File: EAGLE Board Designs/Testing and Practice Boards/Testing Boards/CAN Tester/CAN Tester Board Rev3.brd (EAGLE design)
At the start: 44.1 x 43.2 mm, 10 parts, among them J1 CONNECTOR-CAN_μF_S_RA_, J2 CONNECTOR-2_MICROFIT_SMD_RIGH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, U1 MCP2562FD

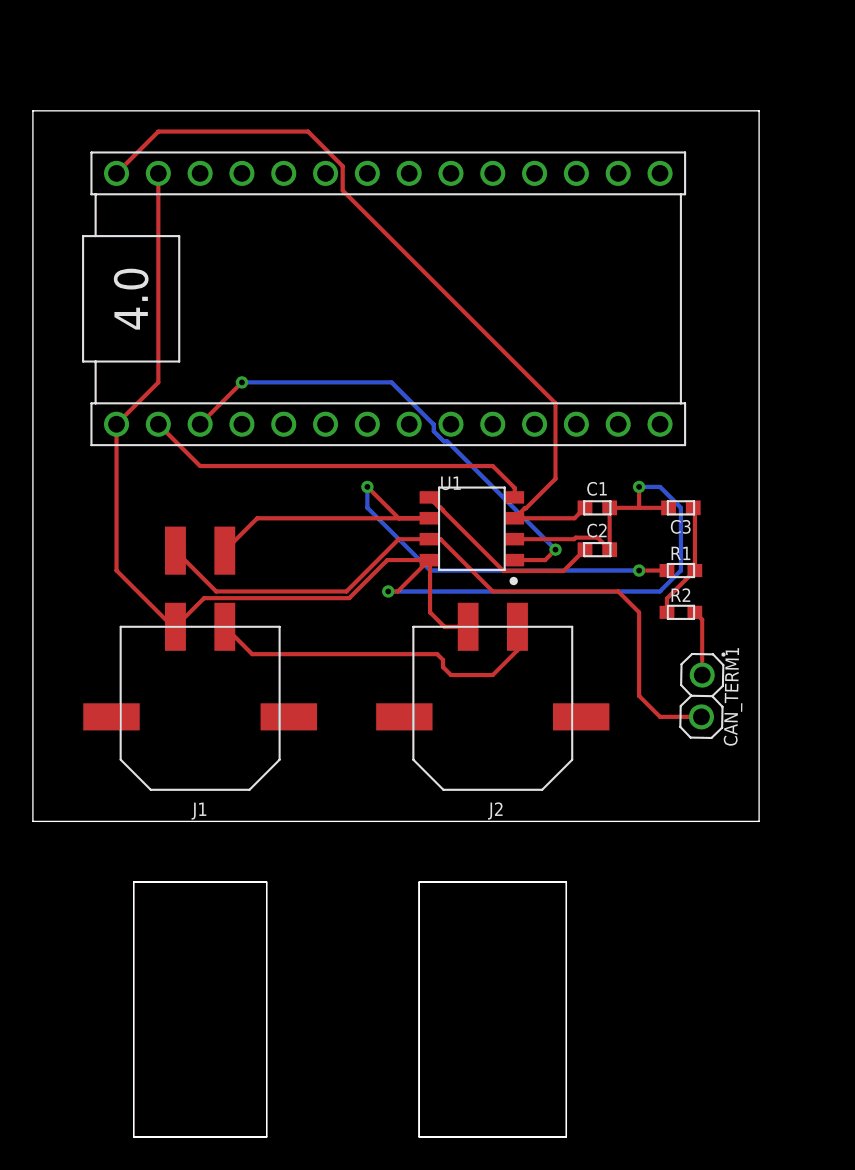
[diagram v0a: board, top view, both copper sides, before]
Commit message: added lin reg
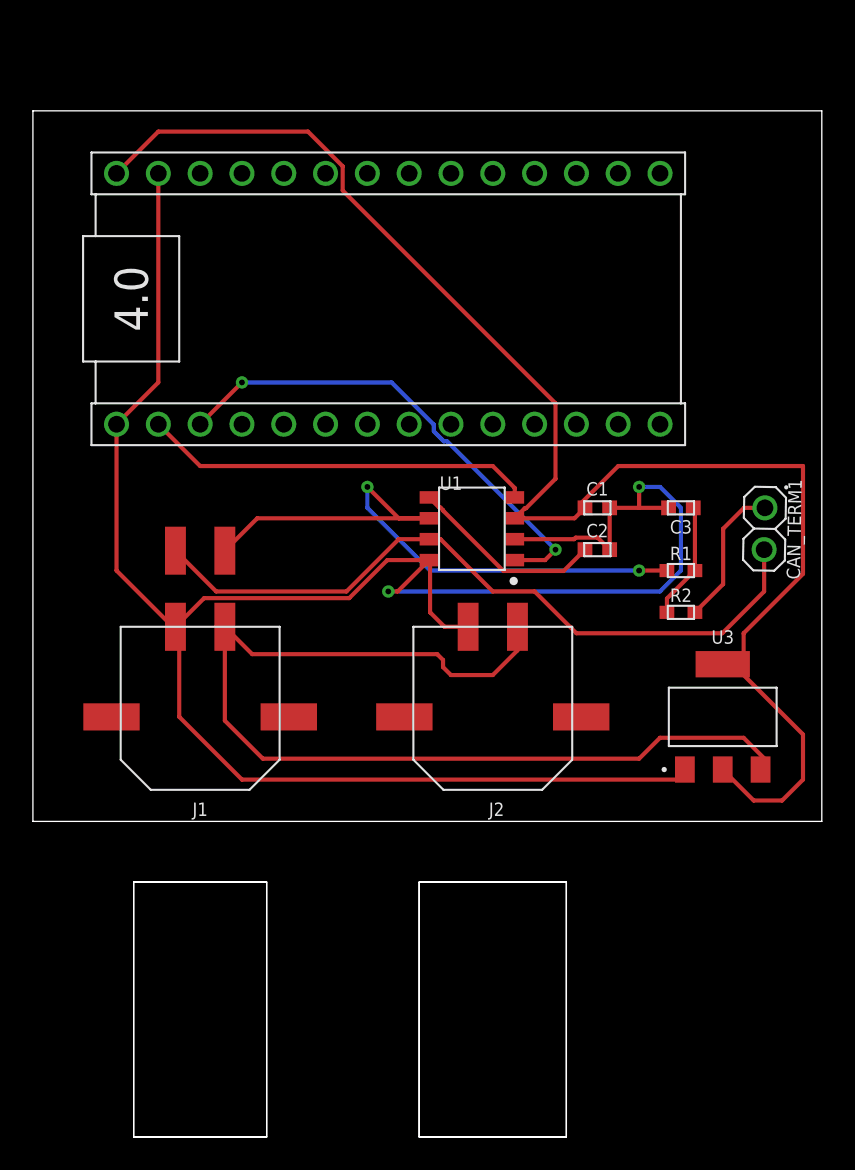
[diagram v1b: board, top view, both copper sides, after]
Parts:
- added U3: VOLTAGE_REGULATOR_SOT-223_3.3V, HyTechDevices:SOT-223
- moved CAN_TERM1 10.9 mm to (44.5, 54.6)
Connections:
- net +12V: now also U3.3
- net +5V: now also U3.2, U3.4
- net GND: now also U3.1
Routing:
- net +5V: track 48.0 -> 91.2 mm
- net +12V: track 21.3 -> 61.8 mm
- net GND: track 95.1 -> 133.4 mm
- net N$5: track 3.99 -> 8.86 mm
- net CANH: track 41.7 -> 44.1 mm
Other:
- board size 44.1 x 43.2 mm -> 47.9 x 43.2 mm
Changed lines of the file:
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@@
 <board>
 <plain>
-<wire x1="0" y1="36.83" x2="44.12" y2="36.83" width="0" layer="20"/>
-<wire x1="44.12" y1="36.83" x2="44.12" y2="80" width="0" layer="20"/>
-<wire x1="44.12" y1="80" x2="0" y2="80" width="0" layer="20"/>
+<wire x1="0" y1="36.83" x2="47.93" y2="36.83" width="0" layer="20"/>
+<wire x1="47.93" y1="36.83" x2="47.93" y2="80" width="0" layer="20"/>
+<wire x1="47.93" y1="80" x2="0" y2="80" width="0" layer="20"/>
 <wire x1="0" y1="80" x2="0" y2="36.83" width="0" layer="20"/>
 </plain>
@@
 <attribute name="VOLTAGE" value="10V" x="10.16" y="95.25" size="1.778" layer="27" rot="R180" display="off"/>
 </element>
-<element name="CAN_TERM1" library="HyTechDevices_Jumper" package="1X02" value="JUMPER__1X02" x="40.64" y="44.45" smashed="yes" rot="R268.9">
-<attribute name="DKPN" value="WM23656-ND" x="0.96030625" y="28.69884375" size="1.778" layer="27" rot="R268.9" display="off"/>
-<attribute name="MANUFACTURER" value="Molex" x="0.96030625" y="28.69884375" size="1.778" layer="27" rot="R268.9" display="off"/>
-<attribute name="MOPN" value="538-90120-1082" x="0.96030625" y="28.69884375" size="1.778" layer="27" rot="R268.9" display="off"/>
-<attribute name="MPN" value="90120-1082 " x="0.96030625" y="28.69884375" size="1.778" layer="27" rot="R268.9" display="off"/>
-<attribute name="NAME" x="42.03674375" y="44.423178125" size="0.8128" layer="25" font="vector" rot="R268.9" align="bottom-center"/>
+<element name="CAN_TERM1" library="HyTechDevices_Jumper" package="1X02" value="JUMPER__1X02" x="44.45" y="54.61" smashed="yes" rot="R268.9">
+<attribute name="DKPN" value="WM23656-ND" x="4.77030625" y="38.85884375" size="1.778" layer="27" rot="R268.9" display="off"/>
+<attribute name="MANUFACTURER" value="Molex" x="4.77030625" y="38.85884375" size="1.778" layer="27" rot="R268.9" display="off"/>
+<attribute name="MOPN" value="538-90120-1082" x="4.77030625" y="38.85884375" size="1.778" layer="27" rot="R268.9" display="off"/>
+<attribute name="MPN" value="90120-1082 " x="4.77030625" y="38.85884375" size="1.778" layer="27" rot="R268.9" display="off"/>
+<attribute name="NAME" x="45.84674375" y="54.583178125" size="0.8128" layer="25" font="vector" rot="R268.9" align="bottom-center"/>
 </element>
 <element name="R1" library="HyTechDevices" package="0603-RES" value="RESISTOR_0603_60.4" x="39.37" y="52.07" smashed="yes">
@@
 <attribute name="MPN" value="0436500214" x="27.94" y="43.18" size="1.778" layer="27" display="off"/>
 <attribute name="NAME" x="28.1686" y="37.973" size="0.8128" layer="25" rot="R180" align="bottom-center"/>
+</element>
+<element name="U3" library="HyTechDevices" package="SOT-223" value="VOLTAGE_REGULATOR_SOT-223_3.3V" x="41.91" y="43.18" smashed="yes">
+<attribute name="DKPN" value="LMS8117AMP-3.3/NOPBCT-ND" x="41.91" y="43.18" size="1.778" layer="27" display="off"/>
+<attribute name="MANUFACTURER" value="Texas Instruments" x="41.91" y="43.18" size="1.778" layer="27" display="off"/>
+<attribute name="MOPN" value="926-LMS8117AMP33NOPB" x="41.91" y="43.18" size="1.778" layer="27" display="off"/>
+<attribute name="MPN" value="LMS8117AMP-3.3/NOPB" x="41.91" y="43.18" size="1.778" layer="27" display="off"/>
+<attribute name="NAME" x="41.91" y="47.625" size="0.8128" layer="25" font="vector" align="bottom-center"/>
 </element>
 </elements>
@@
 <wire x1="39.37" y1="55.88" x2="38.1" y2="57.15" width="0.254" layer="16"/>
 <wire x1="38.1" y1="57.15" x2="36.83" y2="57.15" width="0.254" layer="16"/>
+<contactref element="U3" pad="1"/>
+<wire x1="8.66" y1="48.6537" x2="8.89" y2="48.4237" width="0.254" layer="1"/>
+<wire x1="8.89" y1="48.4237" x2="8.89" y2="43.18" width="0.254" layer="1"/>
+<wire x1="8.89" y1="43.18" x2="12.7" y2="39.37" width="0.254" layer="1"/>
+<wire x1="39.37" y1="39.37" x2="39.61" y2="39.61" width="0.254" layer="1"/>
+<wire x1="39.61" y1="39.61" x2="39.61" y2="39.98" width="0.254" layer="1"/>
+<wire x1="12.7" y1="39.37" x2="39.37" y2="39.37" width="0.254" layer="1"/>
 </signal>
 <signal name="3.3V">
@@
 <contactref element="A1" pad="VIN"/>
 <wire x1="29.2735" y1="55.245" x2="32.905" y2="55.245" width="0.254" layer="1"/>
-<wire x1="32.905" y1="55.245" x2="33.54" y2="55.88" width="0.254" layer="1"/>
+<wire x1="32.905" y1="55.245" x2="33.28" y2="55.62" width="0.254" layer="1"/>
+<wire x1="33.28" y1="55.62" x2="33.54" y2="55.88" width="0.254" layer="1"/>
 <wire x1="5.08" y1="76.2" x2="7.62" y2="78.74" width="0.254" layer="1"/>
 <wire x1="18.8214" y1="75.1586" x2="31.75" y2="62.23" width="0.254" layer="1"/>
@@
 <wire x1="31.75" y1="57.64386875" x2="29.96073125" y2="55.8546" width="0.254" layer="1"/>
 <wire x1="7.62" y1="78.74" x2="16.7127625" y2="78.74" width="0.254" layer="1"/>
+<contactref element="U3" pad="2"/>
+<contactref element="U3" pad="4"/>
+<wire x1="41.91" y1="39.98" x2="43.79" y2="38.1" width="0.254" layer="1"/>
+<wire x1="45.517" y1="38.1" x2="46.787" y2="39.37" width="0.254" layer="1"/>
+<wire x1="46.787" y1="39.37" x2="46.787" y2="42.113" width="0.254" layer="1"/>
+<wire x1="46.787" y1="42.113" x2="43.18" y2="45.72" width="0.254" layer="1"/>
+<wire x1="43.18" y1="45.72" x2="43.18" y2="48.26" width="0.254" layer="1"/>
+<wire x1="43.18" y1="48.26" x2="46.787" y2="51.867" width="0.254" layer="1"/>
+<wire x1="46.787" y1="58.42" x2="35.56" y2="58.42" width="0.254" layer="1"/>
+<wire x1="35.56" y1="58.42" x2="33.28" y2="56.14" width="0.254" layer="1"/>
+<wire x1="33.28" y1="56.14" x2="33.28" y2="55.62" width="0.254" layer="1"/>
+<wire x1="43.79" y1="38.1" x2="45.517" y2="38.1" width="0.254" layer="1"/>
+<wire x1="46.787" y1="51.867" x2="46.787" y2="58.42" width="0.254" layer="1"/>
+<wire x1="41.91" y1="39.98" x2="41.91" y2="46.38" width="0" layer="19" extent="1-1"/>
 </signal>
 <signal name="+3V3">
@@
 <contactref element="CAN_TERM1" pad="2"/>
 <contactref element="J1" pad="4"/>
-<wire x1="24.0665" y1="53.975" x2="24.765" y2="53.975" width="0.254" layer="1"/>
-<wire x1="35.56" y1="50.8" x2="36.83" y2="49.53" width="0.254" layer="1"/>
-<wire x1="36.83" y1="49.53" x2="36.83" y2="44.45" width="0.254" layer="1"/>
-<wire x1="36.83" y1="44.45" x2="38.09976875" y2="43.18023125" width="0.254" layer="1"/>
-<wire x1="38.09976875" y1="43.18023125" x2="40.61561875" y2="43.18023125" width="0.254" layer="1"/>
-<wire x1="24.765" y1="53.975" x2="27.94" y2="50.8" width="0.254" layer="1"/>
-<wire x1="27.94" y1="50.8" x2="35.56" y2="50.8" width="0.254" layer="1"/>
+<wire x1="44.42561875" y1="53.34023125" x2="44.42561875" y2="50.80023125" width="0.254" layer="1"/>
+<wire x1="44.42561875" y1="50.80023125" x2="41.8853875" y2="48.26" width="0.254" layer="1"/>
+<wire x1="33.02" y1="48.26" x2="41.8853875" y2="48.26" width="0.254" layer="1"/>
 <wire x1="8.66" y1="53.2765" x2="11.1365" y2="50.8" width="0.254" layer="1"/>
 <wire x1="22.225" y1="53.975" x2="24.0665" y2="53.975" width="0.254" layer="1"/>
 <wire x1="11.1365" y1="50.8" x2="19.05" y2="50.8" width="0.254" layer="1"/>
 <wire x1="19.05" y1="50.8" x2="22.225" y2="53.975" width="0.254" layer="1"/>
+<wire x1="24.0665" y1="53.975" x2="24.765" y2="53.975" width="0.254" layer="1"/>
+<wire x1="24.765" y1="53.975" x2="27.94" y2="50.8" width="0.254" layer="1"/>
+<wire x1="27.94" y1="50.8" x2="30.48" y2="50.8" width="0.254" layer="1"/>
+<wire x1="30.48" y1="50.8" x2="33.02" y2="48.26" width="0.254" layer="1"/>
 </signal>
 <signal name="CANL">
@@
 <contactref element="R2" pad="2"/>
 <contactref element="CAN_TERM1" pad="1"/>
-<wire x1="40.22" y1="49.53" x2="40.664378125" y2="49.085621875" width="0.254" layer="1"/>
-<wire x1="40.664378125" y1="49.085621875" x2="40.664378125" y2="45.719765625" width="0.254" layer="1"/>
+<wire x1="40.22" y1="49.53" x2="41.934378125" y2="51.244378125" width="0.254" layer="1"/>
+<wire x1="44.474378125" y1="55.879765625" x2="43.204378125" y2="55.879765625" width="0.254" layer="1"/>
+<wire x1="43.204378125" y1="55.879765625" x2="41.934378125" y2="54.609765625" width="0.254" layer="1"/>
+<wire x1="41.934378125" y1="54.609765625" x2="41.934378125" y2="51.244378125" width="0.254" layer="1"/>
 </signal>
 <signal name="+12V">
@@
 <wire x1="13.3237" y1="46.99" x2="24.56360625" y2="46.99" width="0.254" layer="1"/>
 <wire x1="27.94" y1="45.72" x2="29.4386" y2="47.2186" width="0.254" layer="1"/>
+<contactref element="U3" pad="3"/>
+<wire x1="11.66" y1="48.6537" x2="11.66" y2="42.95" width="0.254" layer="1"/>
+<wire x1="11.66" y1="42.95" x2="13.97" y2="40.64" width="0.254" layer="1"/>
+<wire x1="13.97" y1="40.64" x2="36.83" y2="40.64" width="0.254" layer="1"/>
+<wire x1="36.83" y1="40.64" x2="38.1" y2="41.91" width="0.254" layer="1"/>
+<wire x1="38.1" y1="41.91" x2="43.18" y2="41.91" width="0.254" layer="1"/>
+<wire x1="43.18" y1="41.91" x2="44.45" y2="40.64" width="0.254" layer="1"/>
+<wire x1="44.45" y1="40.64" x2="44.21" y2="39.98" width="0" layer="19" extent="1-1"/>
 </signal>
 </signals>

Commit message: made changes to board
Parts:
- removed U3: VOLTAGE_REGULATOR_SOT-223_3.3V, HyTechDevices:SOT-223
- added U2: VOLTAGE_REGULATOR_SOT-89_12V, HyTechDevices:SOT-89
- moved R2 8.03 mm to (41.9, 57.1)
- moved C3 6.48 mm to (33.0, 57.1)
- moved C1 5.24 mm to (29.2, 57.1)
- moved C2 5.24 mm to (29.2, 54.6)
- moved R1 5.24 mm to (38.1, 57.1), turned to 180 degrees
- moved U1 3.81 mm to (22.9, 54.6), turned to 180 degrees
- moved CAN_TERM1 3.59 mm to (41.9, 52.1), turned to 178.9 degrees
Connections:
- removed net 3.3V: A1.3.3V
- net +12V: now also U2.1; no longer U3.3
- net +3V3: now also A1.3.3V
- net +5V: now also U2.3; no longer U3.2, U3.4
- net GND: now also U2.2; no longer U3.1
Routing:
- net GND: track 133.4 -> 17.2 mm, vias 2 -> 6
- net +3V3: track 11.9 -> 57.4 mm
- net +12V: track 61.8 -> 31.7 mm
- net 4.0_CTX: track 29.8 -> 16.2 mm, vias 2 -> 0
- net +5V: track 91.2 -> 79.4 mm
- net CANH: track 44.1 -> 34.4 mm
- net 4.0_CRX: track 23.8 -> 14.9 mm
- net CANL: track 38.8 -> 31.0 mm, vias 2 -> 0
- net N$5: track 8.86 -> 5.28 mm
- net N$3: track 7.10 -> 7.85 mm
- added copper zone on layer 16, net GND
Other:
- board text added: "HyTech Racing 2022 CAN Tester Board rev3 Designed by Brendan Bassett"
